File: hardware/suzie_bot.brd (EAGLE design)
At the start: 98.7 x 71.1 mm, 40 parts, among them IC1 LT1529CT33, IC2 L9637D, IC3 IC_TXB0108-TSSOP-20, U1 ATMEGA1284P-AU, Y1 14.7456, Y2 6.0, Y3 16.0

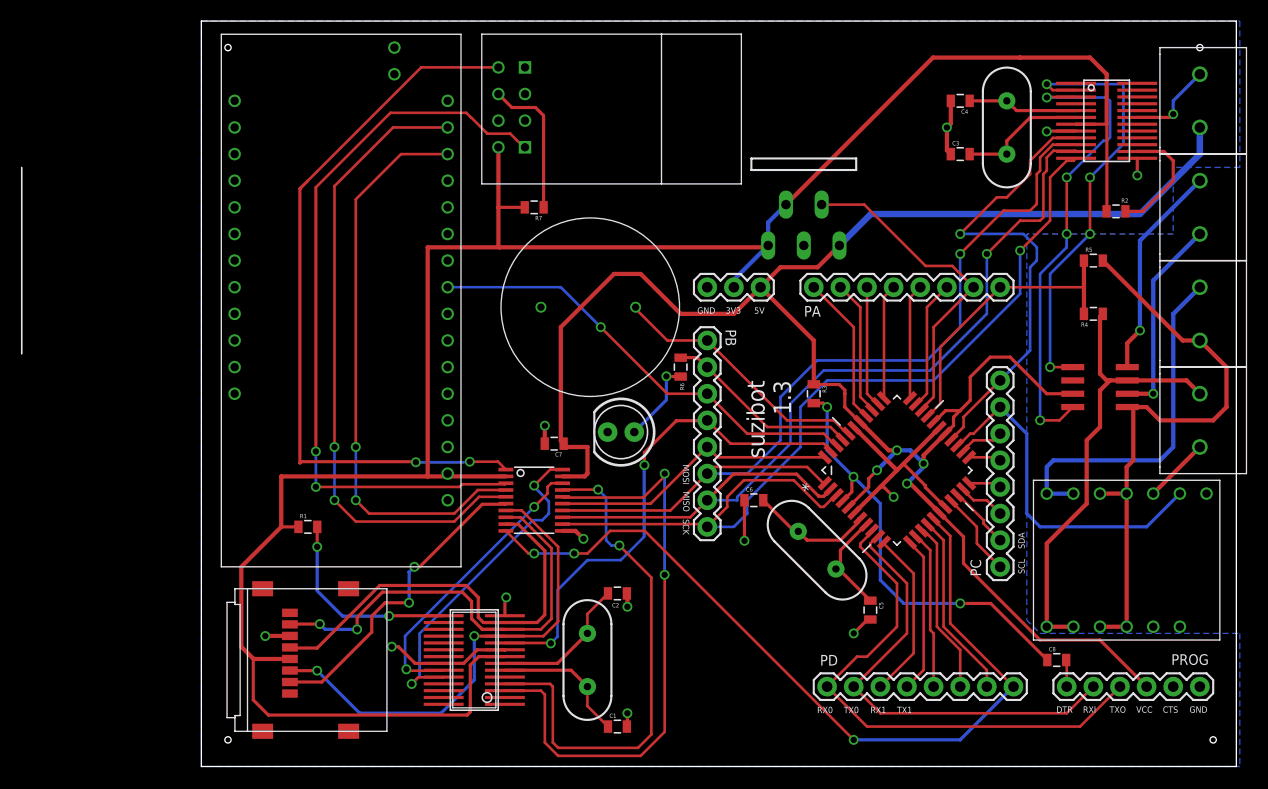
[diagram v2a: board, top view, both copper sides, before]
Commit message: Much better decoupling; adding TI TPS2113A for limiting inrush current.
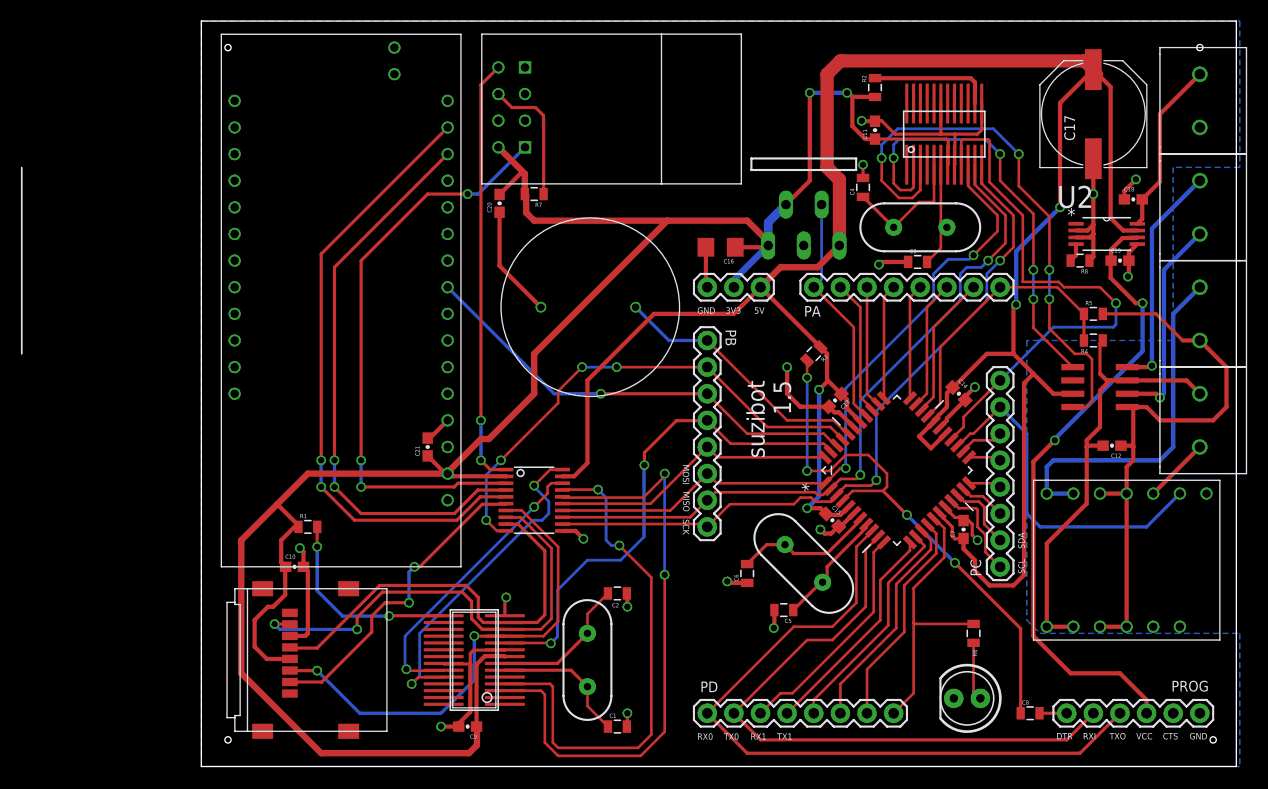
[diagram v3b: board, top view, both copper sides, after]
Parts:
- added C10, C11, C12, C13, C14, C15, C18, C19, C20, C21, C9: 0.1uF, SparkFun-Capacitors:0603-CAP
- added C16: 22uF, SparkFun-Capacitors:1206
- added C17: 1000uF, rcl:PANASONIC_G
- added R8: 500, SparkFun-Passives:0805
- added U2: TPS2113APWR, Texas Instruments_By_element14_Batch_1:SOP65P640X120-8N
- C7: device SparkFun-Passives:0805 -> SparkFun-Capacitors:0603-CAP
- moved D1 41.7 mm to (73.0, 6.50)
- moved C7 39.9 mm to (72.7, 22.6), turned to 90 degrees
- moved R6 37.8 mm to (73.7, 12.7)
- moved R2 25.8 mm to (64.3, 64.8), turned to 90 degrees
- moved U$7 15.5 mm to (70.9, 60.3), turned to 0 degrees
- moved Y2 12.6 mm to (68.6, 51.4), turned to 180 degrees
- moved C4 12.4 mm to (63.1, 55.2), turned to 90 degrees
- moved PD0-7 11.7 mm to (48.3, 5.08)
- moved C3 11.1 mm to (68.3, 48.1)
- moved C5 8.26 mm to (55.6, 14.9), turned to 180 degrees
- moved C6 7.01 mm to (52.1, 18.4), turned to 90 degrees
- moved C8 5.68 mm to (79.1, 5.08)
- moved R5 5.08 mm to (85.1, 43.2)
- moved R3 3.81 mm to (58.4, 39.4), turned to 225 degrees
- moved PROGRAMMER 2.54 mm to (82.5, 5.08)
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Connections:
- removed net N$2 (its old number): PB0-7.2, R6.1, U1.41
- removed net PA6: IC1.4, PA0-7.7, U1.31
- new net N$25: IC3.OE, PB0-7.2, U1.41
- new net N$27: PA0-7.7, U1.31
- new net N$30: C19.1, PROGRAMMER.4, U2.6
- new net N$31: R8.2, U2.4
- new net N$32: 5V/GND.P$2, C18.2, U2.8
- net 12V-OUT: now also C12.2
- net 3V3: now also C10.1, C11.1, C16.1, C20.2, C21.1, C9.1
- net 5V: now also C13.1, C14.1, C15.1, C17.+, U2.7; no longer 5V/GND.P$1, PROGRAMMER.4
- net EXTGND: now also C12.1
- net GND: now also 5V/GND.P$1, C10.2, C11.2, C13.2, C14.2, C15.2, C16.2, C17.-, C18.1, C19.2, C20.1, C21.2, C9.2, R8.1, U2.2, U2.3, U2.5; no longer 5V/GND.P$2
- net PA0: now also IC1.4
- net PD7: now also R6.1; no longer IC3.OE
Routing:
- net N$30: track 0.00 -> 60.4 mm, vias 0 -> 2
- net PD7: track 79.7 -> 26.8 mm, vias 3 -> 0
- net GND: track 71.8 -> 121.9 mm, vias 14 -> 18
- net N$25: track 0.00 -> 48.4 mm, vias 0 -> 4
- net 5V: track 185.4 -> 223.1 mm
- net PA6: track 31.5 -> 0.00 mm
- net N$5: track 70.0 -> 40.9 mm
- net PB6/MISO: track 86.4 -> 67.7 mm, vias 1 -> 2
- net N$2 (its old number): track 18.7 -> 0.00 mm
- net PB7/SCLK: track 87.7 -> 69.1 mm, vias 1 -> 2
- net PB5/MOSI: track 84.5 -> 66.8 mm, vias 1 -> 2
- net N$PD0/RXD0: track 51.2 -> 68.6 mm
- net PD1/TXD0: track 43.2 -> 60.4 mm
- net N$32: track 0.00 -> 16.7 mm
- net N$8: track 71.1 -> 55.7 mm, vias 2 -> 3
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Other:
- board text added: "6 November 2016"
- board text added: "suzibot 1.5"
- board text removed: "17 October 2016"
- board text removed: "suzibot 1.3"

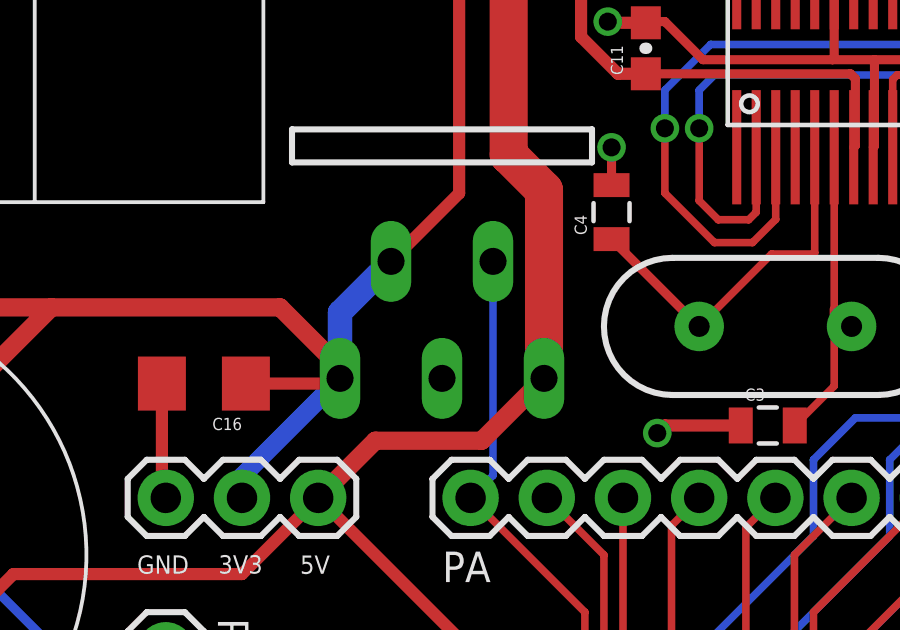
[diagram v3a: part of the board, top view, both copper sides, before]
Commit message: Adding 1k pullup resistor for disabling 3V3 regulator until MC-enabled.
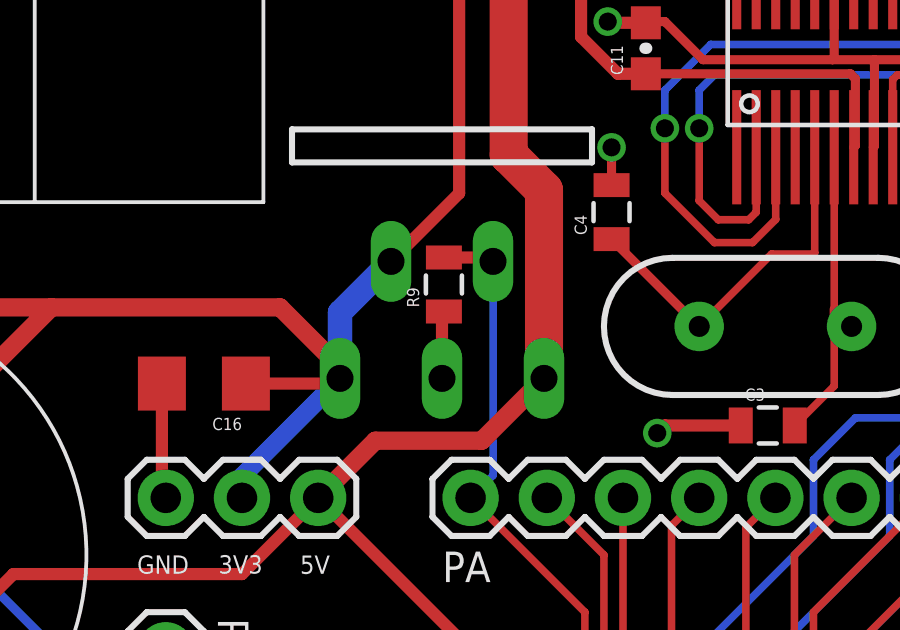
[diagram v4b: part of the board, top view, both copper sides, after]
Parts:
- added R9: 1k, SparkFun-Passives:0805
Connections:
- net GND: now also R9.1
- net PA0: now also R9.2
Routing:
- net GND: track 121.9 -> 124.2 mm
- net PA0: track 22.6 -> 24.3 mm
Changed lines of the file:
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@@
 <element name="C20" library="SparkFun-Capacitors" package="0603-CAP" value="0.1uF" x="28.448" y="53.721" rot="R90"/>
 <element name="C21" library="SparkFun-Capacitors" package="0603-CAP" value="0.1uF" x="21.59" y="30.48" rot="R90"/>
+<element name="R9" library="SparkFun-Passives" package="0805" value="1k" x="57.531" y="52.832" rot="R90"/>
 </elements>
 <signals>
@@
 <wire x1="21.59" y1="31.33" x2="21.805" y2="31.33" width="0.4064" layer="1"/>
 <wire x1="21.805" y1="31.33" x2="23.495" y2="33.02" width="0.4064" layer="1"/>
+<contactref element="R9" pad="1"/>
+<wire x1="57.531" y1="51.932" x2="57.4675" y2="51.932" width="0.4064" layer="1"/>
+<wire x1="57.4675" y1="51.932" x2="57.4675" y2="49.7025" width="0.4064" layer="1"/>
 </signal>
 <signal name="3V3" class="1">
@@
 <wire x1="59.1675" y1="53.6025" x2="59.1675" y2="46.4675" width="0.254" layer="16"/>
 <wire x1="59.1675" y1="46.4675" x2="58.42" y2="45.72" width="0.254" layer="16"/>
+<contactref element="R9" pad="2"/>
+<wire x1="57.531" y1="53.732" x2="59.1675" y2="53.732" width="0.4064" layer="1"/>
+<wire x1="59.1675" y1="53.732" x2="59.1675" y2="53.6025" width="0.4064" layer="1"/>
 </signal>
 <signal name="N$30">

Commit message: Updating to latest board version.
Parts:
- added R10, R11: 10k, SparkFun-Passives:0805
- moved R7 3.19 mm to (28.8, 53.3), turned to 90 degrees
- moved C20 2.34 mm to (30.7, 53.2)
- moved C16 0.77 mm to (49.4, 50.3)
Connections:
- net 3V3: now also R10.1, U$2.!RESET, U$7.!RESET
- net 5V: now also R11.2
- net GND: now also R10.2, R11.1
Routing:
- net 5V: track 223.1 -> 226.2 mm
- net GND: track 124.2 -> 125.9 mm, vias 18 -> 19
- net 3V3: track 215.6 -> 216.8 mm
- net N$4: track 12.6 -> 13.6 mm
